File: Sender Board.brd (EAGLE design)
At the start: 38.1 x 38.1 mm, 11 parts, among them IC2 PIC16F1826/27SO, J1 PIC_ICSP_MINI_5_PIN, U1 915MHz, X1 87758-0216, X2 BU-SMA-V

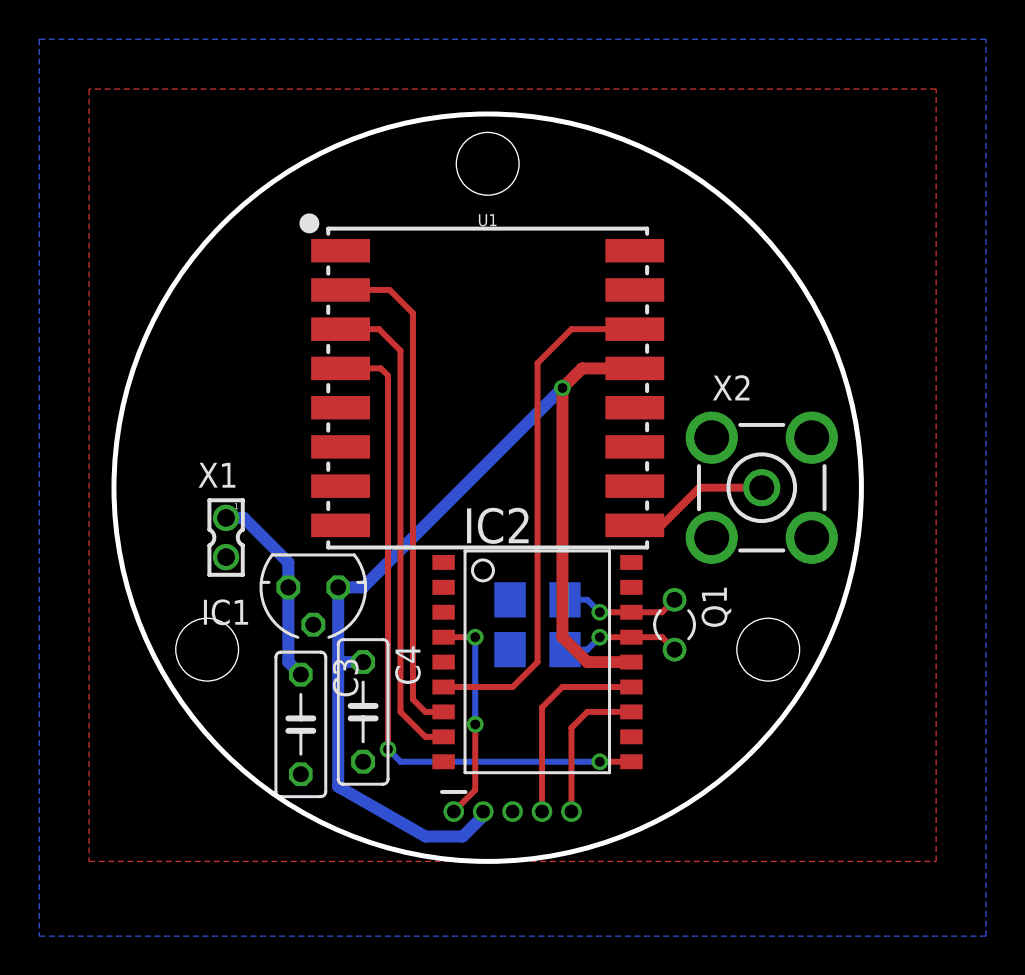
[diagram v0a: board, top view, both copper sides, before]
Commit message: Ordered sender PCB
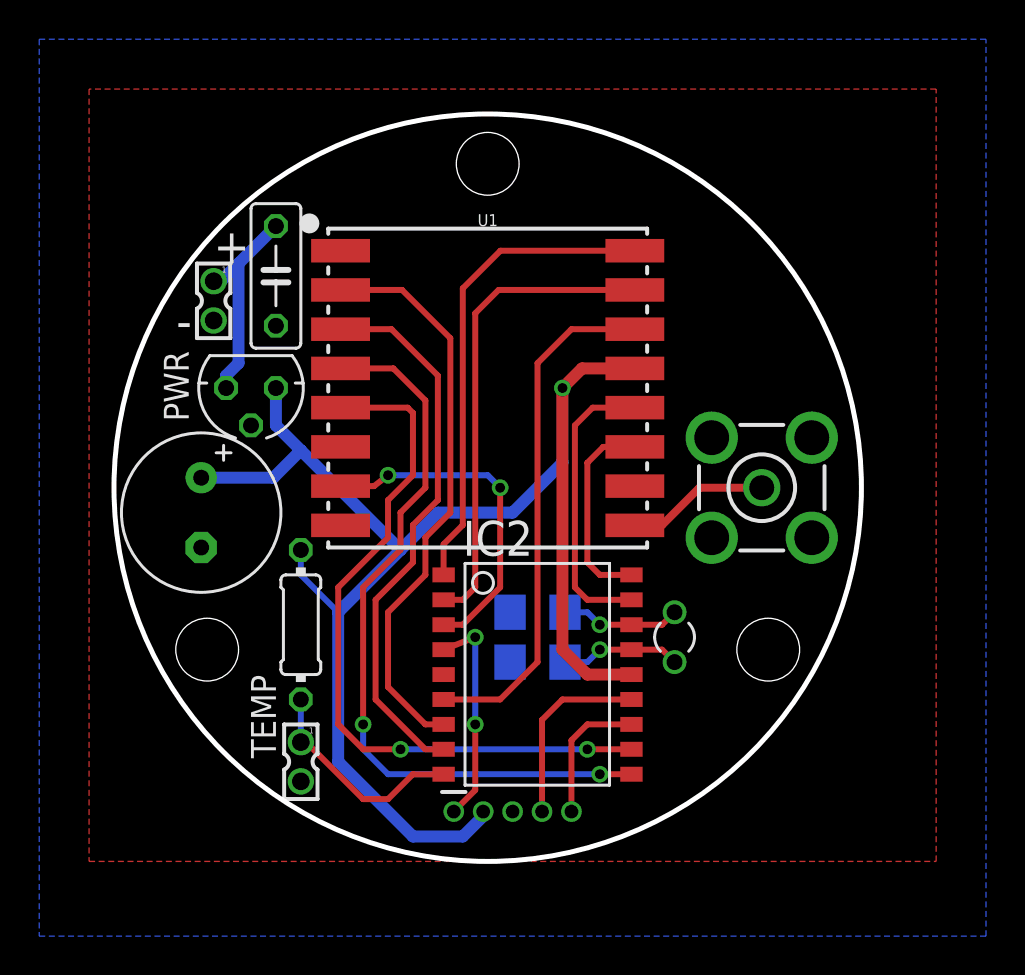
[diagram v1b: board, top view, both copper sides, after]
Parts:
- removed X1: 87758-0216, con-molex:87758-0216
- added PWR, TEMP: 87758-0216, con-molex:87758-0216
- added R1: (no value), resistor:0204/7
- C4: device resistor:C050-025X075 -> resistor:E3,5-8
- moved C3 22.9 mm to (8.26, 29.8)
- moved C4 13.1 mm to (4.45, 17.8)
- moved IC1 10.6 mm to (6.99, 24.1)
- moved C1 0.64 mm to (21.6, 12.7)
- moved C2 0.63 mm to (21.6, 10.2)
- moved IC2 0.63 mm to (21.6, 9.53)
- moved Q1 0.63 mm to (28.6, 11.4)
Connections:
- net N$4 renamed MISO
- net N$5 renamed MOSI
- net N$6 renamed SCK
- removed net +5V: C3.1, IC1.IN, X1.1
- new net +12V: C3.1, IC1.IN, PWR.1
- new net N$11: IC2.9, R1.1, TEMP.1
- new net N$12: IC2.11, U1.5
- new net N$13: IC2.18, U1.11
- new net N$14: IC2.17, U1.12
- new net N$15: IC2.1, U1.16
- new net N$16: IC2.2, U1.15
- new net N$17: IC2.3, U1.7
- net +3V3: now also C4.+, R1.2; no longer C4.1
- net GND: now also C4.-, PWR.2, TEMP.2; no longer C4.2, X1.2
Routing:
- net N$12: track 0.00 -> 36.7 mm, vias 0 -> 2
- net N$15: track 0.00 -> 24.6 mm
- net N$16: track 0.00 -> 24.5 mm
- net +3V3: track 56.6 -> 77.6 mm
- net N$17: track 0.00 -> 17.3 mm, vias 0 -> 2
- net N$14: track 0.00 -> 14.8 mm
- net N$11: track 0.00 -> 11.2 mm
- net +12V: track 0.00 -> 11.0 mm
- net N$13: track 0.00 -> 10.3 mm
- net +5V: track 10.1 -> 0.00 mm
- net SCK: track 34.3 -> 38.3 mm
- net MOSI: track 24.6 -> 28.3 mm
- net MISO: track 25.7 -> 29.3 mm
- net N$2: track 7.66 -> 7.03 mm
- net N$1: track 10.3 -> 9.66 mm
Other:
- board text added: "+"
- board text added: "-"
